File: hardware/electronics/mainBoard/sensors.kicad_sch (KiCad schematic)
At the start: 8 parts, among them J16 M8S-04PFFR-SF8001, J17 STEMMA-QT, J18 STEMMA-QT, J19 STEMMA-QT, J20 STEMMA-QT, J21 STEMMA-QT, U18 LPS28DFW

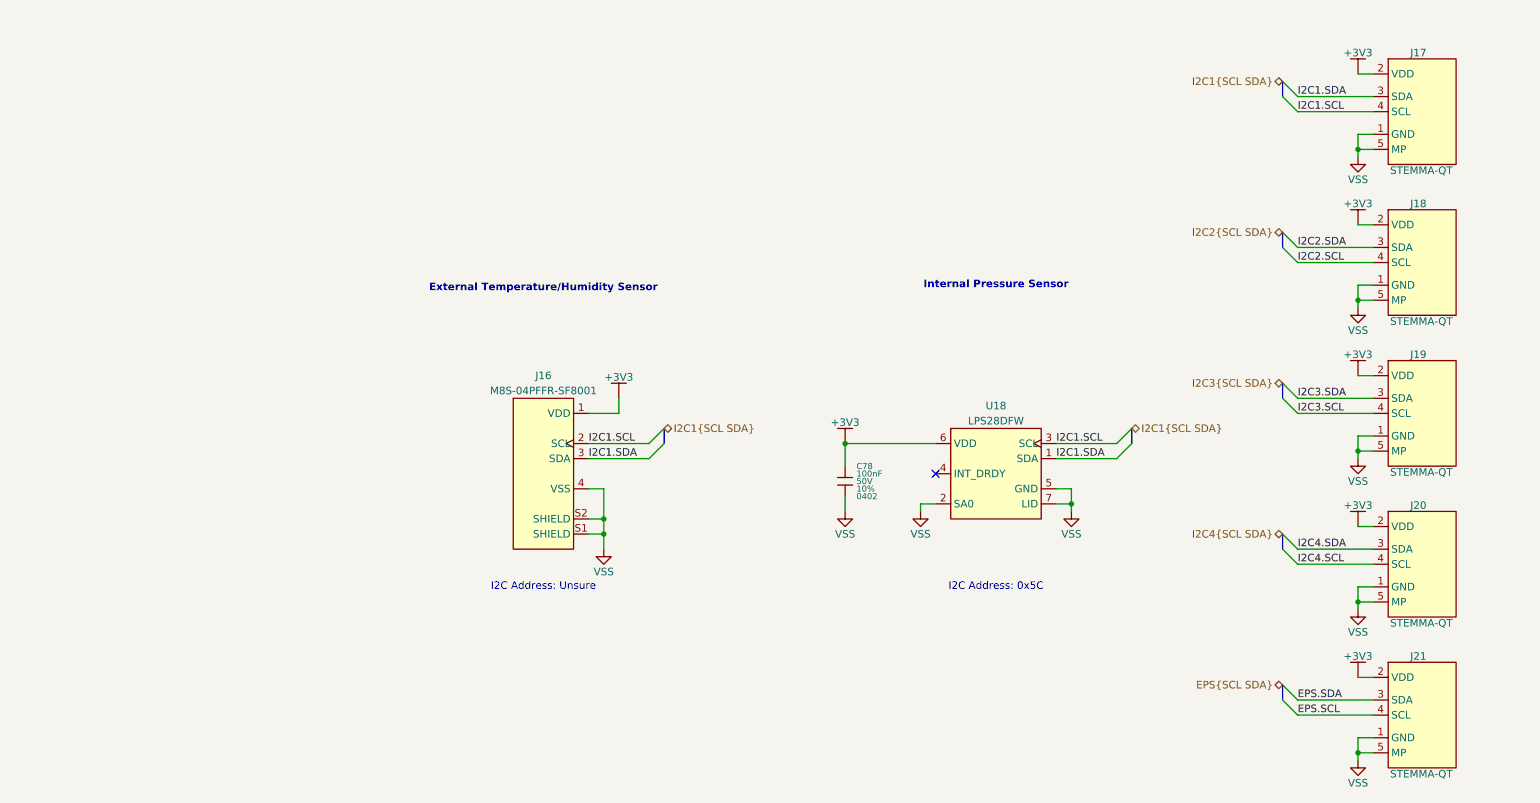
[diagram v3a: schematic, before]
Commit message: updated symbol refs
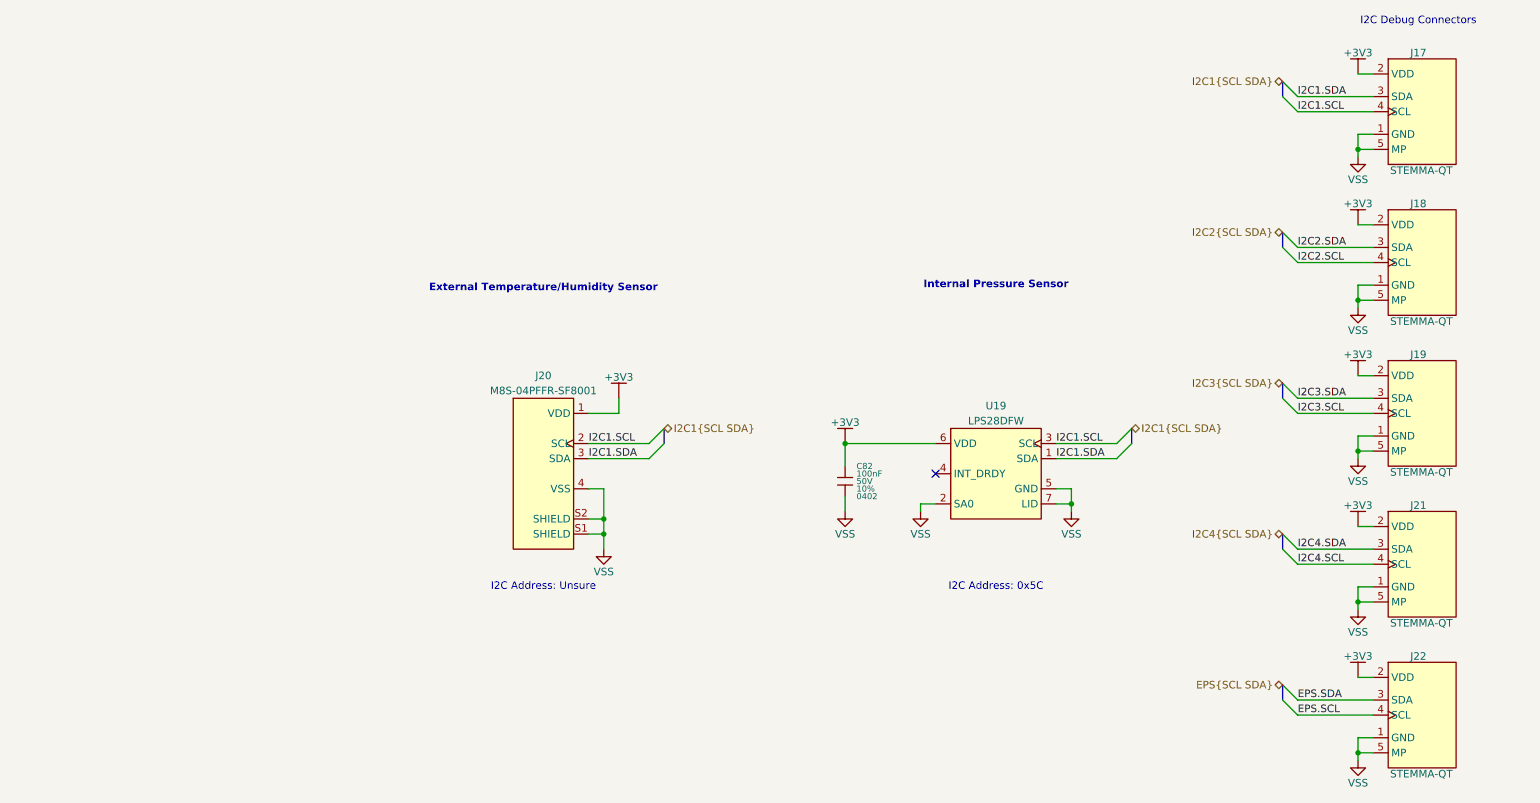
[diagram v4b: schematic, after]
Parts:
- renumbered C78 to C82, J16 to J20, J20 to J21, J21 to J22, U18 to U19
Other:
- note added: "I2C Debug Connectors"
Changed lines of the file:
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@@
+		)
+	)
+	(text "I2C Debug Connectors"
+		(exclude_from_sim no)
+		(at 248.92 31.75 0)
+		(effects
+			(font
+				(size 1.27 1.27)
+			)
 		)
 	)
@@
 		(dnp no)
 		(fields_autoplaced yes)
-		(property "Reference" "#PWR0187"
+		(property "Reference" "#PWR0186"
 			(at 238.76 54.61 0)
 			(effects
@@
 			(project "mainBoard"
 				(path "/be16e32f-2ccf-4272-9ec7-94d5fe7a55e0/4fa91b0b-0224-4171-b5d2-5ca4be681229"
-					(reference "#PWR0187")
+					(reference "#PWR0186")
 					(unit 1)
 				)
@@
 	)
 	(symbol
-		(lib_name "STEMMA-QT_1")
 		(lib_id "lib_sch:STEMMA-QT_1")
 		(at 246.38 148.59 0)
@@
 		(dnp no)
 		(fields_autoplaced yes)
-		(property "Reference" "J21"
+		(property "Reference" "J22"
 			(at 248.92 138.684 0)
 			(do_not_autoplace yes)
@@
 			(project "mainBoard"
 				(path "/be16e32f-2ccf-4272-9ec7-94d5fe7a55e0/4fa91b0b-0224-4171-b5d2-5ca4be681229"
-					(reference "J21")
+					(reference "J22")
 					(unit 1)
 				)
@@
 		(dnp no)
 		(fields_autoplaced yes)
-		(property "Reference" "#PWR0180"
+		(property "Reference" "#PWR0197"
 			(at 111.76 120.65 0)
 			(effects
@@
 			(project "mainBoard"
 				(path "/be16e32f-2ccf-4272-9ec7-94d5fe7a55e0/4fa91b0b-0224-4171-b5d2-5ca4be681229"
-					(reference "#PWR0180")
+					(reference "#PWR0197")
 					(unit 1)
 				)
@@
 	)
 	(symbol
-		(lib_name "STEMMA-QT_1")
 		(lib_id "lib_sch:STEMMA-QT_1")
 		(at 246.38 72.39 0)
@@
 	)
 	(symbol
-		(lib_name "STEMMA-QT_1")
 		(lib_id "lib_sch:STEMMA-QT_1")
 		(at 246.38 46.99 0)
@@
 	)
 	(symbol
-		(lib_name "STEMMA-QT_1")
 		(lib_id "lib_sch:STEMMA-QT_1")
 		(at 246.38 97.79 0)
@@
 		(dnp no)
 		(fields_autoplaced yes)
-		(property "Reference" "#PWR0193"
+		(property "Reference" "#PWR0198"
 			(at 238.76 130.81 0)
 			(effects
@@
 			(project "mainBoard"
 				(path "/be16e32f-2ccf-4272-9ec7-94d5fe7a55e0/4fa91b0b-0224-4171-b5d2-5ca4be681229"
-					(reference "#PWR0193")
+					(reference "#PWR0198")
 					(unit 1)
 				)
@@
 		(dnp no)
 		(fields_autoplaced yes)
-		(property "Reference" "#PWR0190"
+		(property "Reference" "#PWR0189"
 			(at 238.76 91.44 0)
 			(effects
@@
 			(project "mainBoard"
 				(path "/be16e32f-2ccf-4272-9ec7-94d5fe7a55e0/4fa91b0b-0224-4171-b5d2-5ca4be681229"
-					(reference "#PWR0190")
+					(reference "#PWR0189")
 					(unit 1)
 				)
@@
 		(dnp no)
 		(fields_autoplaced yes)
-		(property "Reference" "#PWR0195"
+		(property "Reference" "#PWR0200"
 			(at 238.76 156.21 0)
 			(effects
@@
 			(project "mainBoard"
 				(path "/be16e32f-2ccf-4272-9ec7-94d5fe7a55e0/4fa91b0b-0224-4171-b5d2-5ca4be681229"
-					(reference "#PWR0195")
+					(reference "#PWR0200")
 					(unit 1)
 				)
@@
 		(dnp no)
 		(fields_autoplaced yes)
-		(property "Reference" "#PWR0194"
+		(property "Reference" "#PWR0199"
 			(at 238.76 142.24 0)
 			(effects
@@
 			(project "mainBoard"
 				(path "/be16e32f-2ccf-4272-9ec7-94d5fe7a55e0/4fa91b0b-0224-4171-b5d2-5ca4be681229"
-					(reference "#PWR0194")
+					(reference "#PWR0199")
 					(unit 1)
 				)
@@
 		(dnp no)
 		(fields_autoplaced yes)
-		(property "Reference" "#PWR0189"
+		(property "Reference" "#PWR0188"
 			(at 238.76 80.01 0)
 			(effects
@@
 			(project "mainBoard"
 				(path "/be16e32f-2ccf-4272-9ec7-94d5fe7a55e0/4fa91b0b-0224-4171-b5d2-5ca4be681229"
-					(reference "#PWR0189")
+					(reference "#PWR0188")
 					(unit 1)
 				)
@@
 		(dnp no)
 		(fields_autoplaced yes)
-		(property "Reference" "#PWR0188"
+		(property "Reference" "#PWR0187"
 			(at 238.76 66.04 0)
 			(effects
@@
 			(project "mainBoard"
 				(path "/be16e32f-2ccf-4272-9ec7-94d5fe7a55e0/4fa91b0b-0224-4171-b5d2-5ca4be681229"
-					(reference "#PWR0188")
+					(reference "#PWR0187")
 					(unit 1)
 				)
@@
 		(dnp no)
 		(fields_autoplaced yes)
-		(property "Reference" "#PWR0183"
+		(property "Reference" "#PWR0193"
 			(at 152.4 114.3 0)
 			(effects
@@
 			(project "mainBoard"
 				(path "/be16e32f-2ccf-4272-9ec7-94d5fe7a55e0/4fa91b0b-0224-4171-b5d2-5ca4be681229"
-					(reference "#PWR0183")
+					(reference "#PWR0193")
 					(unit 1)
 				)
@@
 		(dnp no)
 		(fields_autoplaced yes)
-		(property "Reference" "C78"
+		(property "Reference" "C82"
 			(at 154.305 106.68 0)
 			(do_not_autoplace yes)
@@
 			(project "mainBoard"
 				(path "/be16e32f-2ccf-4272-9ec7-94d5fe7a55e0/4fa91b0b-0224-4171-b5d2-5ca4be681229"
-					(reference "C78")
+					(reference "C82")
 					(unit 1)
 				)
@@
 	)
 	(symbol
-		(lib_name "STEMMA-QT_1")
 		(lib_id "lib_sch:STEMMA-QT_1")
 		(at 246.38 123.19 0)
@@
 		(dnp no)
 		(fields_autoplaced yes)
-		(property "Reference" "J20"
+		(property "Reference" "J21"
 			(at 248.92 113.284 0)
 			(do_not_autoplace yes)
@@
 			(project "mainBoard"
 				(path "/be16e32f-2ccf-4272-9ec7-94d5fe7a55e0/4fa91b0b-0224-4171-b5d2-5ca4be681229"
-					(reference "J20")
+					(reference "J21")
 					(unit 1)
 				)
@@
 		(dnp no)
 		(fields_autoplaced yes)
-		(property "Reference" "#PWR0191"
+		(property "Reference" "#PWR0192"
 			(at 238.76 105.41 0)
 			(effects
@@
 			(project "mainBoard"
 				(path "/be16e32f-2ccf-4272-9ec7-94d5fe7a55e0/4fa91b0b-0224-4171-b5d2-5ca4be681229"
-					(reference "#PWR0191")
+					(reference "#PWR0192")
 					(unit 1)
 				)
@@
 		(dnp no)
 		(fields_autoplaced yes)
-		(property "Reference" "#PWR0181"
+		(property "Reference" "#PWR0190"
 			(at 114.3 95.25 0)
 			(effects
@@
 			(project "mainBoard"
 				(path "/be16e32f-2ccf-4272-9ec7-94d5fe7a55e0/4fa91b0b-0224-4171-b5d2-5ca4be681229"
-					(reference "#PWR0181")
+					(reference "#PWR0190")
 					(unit 1)
 				)
@@
 		(dnp no)
 		(fields_autoplaced yes)
-		(property "Reference" "J16"
+		(property "Reference" "J20"
 			(at 101.6 91.44 0)
 			(do_not_autoplace yes)
@@
 			(project "mainBoard"
 				(path "/be16e32f-2ccf-4272-9ec7-94d5fe7a55e0/4fa91b0b-0224-4171-b5d2-5ca4be681229"
-					(reference "J16")
+					(reference "J20")
 					(unit 1)
 				)
@@
 		(dnp no)
 		(fields_autoplaced yes)
-		(property "Reference" "#PWR0192"
+		(property "Reference" "#PWR0196"
 			(at 238.76 116.84 0)
 			(effects
@@
 			(project "mainBoard"
 				(path "/be16e32f-2ccf-4272-9ec7-94d5fe7a55e0/4fa91b0b-0224-4171-b5d2-5ca4be681229"
-					(reference "#PWR0192")
+					(reference "#PWR0196")
 					(unit 1)
 				)
@@
 		(dnp no)
 		(fields_autoplaced yes)
-		(property "Reference" "#PWR0185"
+		(property "Reference" "#PWR0195"
 			(at 190.5 114.3 0)
 			(effects
@@
 			(project "mainBoard"
 				(path "/be16e32f-2ccf-4272-9ec7-94d5fe7a55e0/4fa91b0b-0224-4171-b5d2-5ca4be681229"
-					(reference "#PWR0185")
+					(reference "#PWR0195")
 					(unit 1)
 				)
@@
 		(dnp no)
 		(fields_autoplaced yes)
-		(property "Reference" "U18"
+		(property "Reference" "U19"
 			(at 177.8 96.52 0)
 			(do_not_autoplace yes)
@@
 			(project "mainBoard"
 				(path "/be16e32f-2ccf-4272-9ec7-94d5fe7a55e0/4fa91b0b-0224-4171-b5d2-5ca4be681229"
-					(reference "U18")
+					(reference "U19")
 					(unit 1)
 				)
@@
 		(dnp no)
 		(fields_autoplaced yes)
-		(property "Reference" "#PWR0182"
+		(property "Reference" "#PWR0191"
 			(at 152.4 102.87 0)
 			(effects
@@
 			(project "mainBoard"
 				(path "/be16e32f-2ccf-4272-9ec7-94d5fe7a55e0/4fa91b0b-0224-4171-b5d2-5ca4be681229"
-					(reference "#PWR0182")
+					(reference "#PWR0191")
 					(unit 1)
 				)
@@
 		(dnp no)
 		(fields_autoplaced yes)
-		(property "Reference" "#PWR0184"
+		(property "Reference" "#PWR0194"
 			(at 165.1 114.3 0)
 			(effects
@@
 			(project "mainBoard"
 				(path "/be16e32f-2ccf-4272-9ec7-94d5fe7a55e0/4fa91b0b-0224-4171-b5d2-5ca4be681229"
-					(reference "#PWR0184")
+					(reference "#PWR0194")
 					(unit 1)
 				)
@@
 		(dnp no)
 		(fields_autoplaced yes)
-		(property "Reference" "#PWR0186"
+		(property "Reference" "#PWR0185"
 			(at 238.76 40.64 0)
 			(effects
@@
 			(project "mainBoard"
 				(path "/be16e32f-2ccf-4272-9ec7-94d5fe7a55e0/4fa91b0b-0224-4171-b5d2-5ca4be681229"
-					(reference "#PWR0186")
+					(reference "#PWR0185")
 					(unit 1)
 				)

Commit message: assigned FPs
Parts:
- J17, J18, J19, J21, J22: footprint (none) -> lib_connectors:JST_SH_BM04B-SRSS-TB
- J20: footprint (none) -> lib_connectors:M8S-04PFFR-SF8001
- U19: footprint (none) -> lib_ICs:CCLGA7_LPS28DFWTR
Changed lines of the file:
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@@
 			)
 		)
-		(property "Footprint" ""
+		(property "Footprint" "lib_connectors:JST_SH_BM04B-SRSS-TB"
 			(at 241.3 142.24 0)
 			(effects
@@
 			)
 		)
-		(property "Footprint" ""
+		(property "Footprint" "lib_connectors:JST_SH_BM04B-SRSS-TB"
 			(at 241.3 66.04 0)
 			(effects
@@
 			)
 		)
-		(property "Footprint" ""
+		(property "Footprint" "lib_connectors:JST_SH_BM04B-SRSS-TB"
 			(at 241.3 40.64 0)
 			(effects
@@
 			)
 		)
-		(property "Footprint" ""
+		(property "Footprint" "lib_connectors:JST_SH_BM04B-SRSS-TB"
 			(at 241.3 91.44 0)
 			(effects
@@
 			)
 		)
-		(property "Footprint" ""
+		(property "Footprint" "lib_connectors:JST_SH_BM04B-SRSS-TB"
 			(at 241.3 116.84 0)
 			(effects
@@
 			)
 		)
-		(property "Footprint" ""
+		(property "Footprint" "lib_connectors:M8S-04PFFR-SF8001"
 			(at 101.6 107.95 0)
 			(effects
@@
 			)
 		)
-		(property "Footprint" ""
+		(property "Footprint" "lib_ICs:CCLGA7_LPS28DFWTR"
 			(at 177.8 107.95 0)
 			(effects

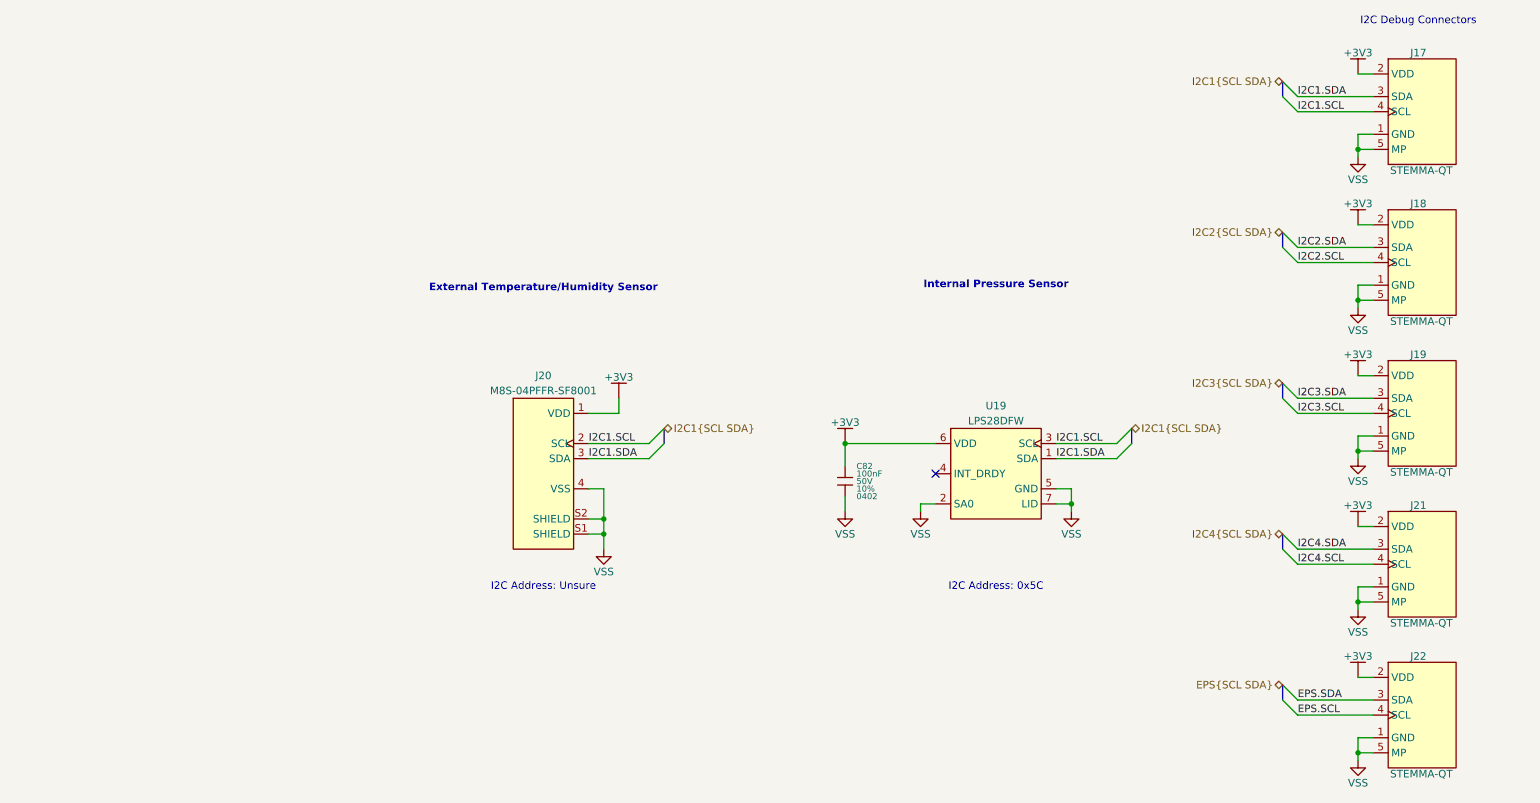
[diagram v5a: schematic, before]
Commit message: assigned footprints
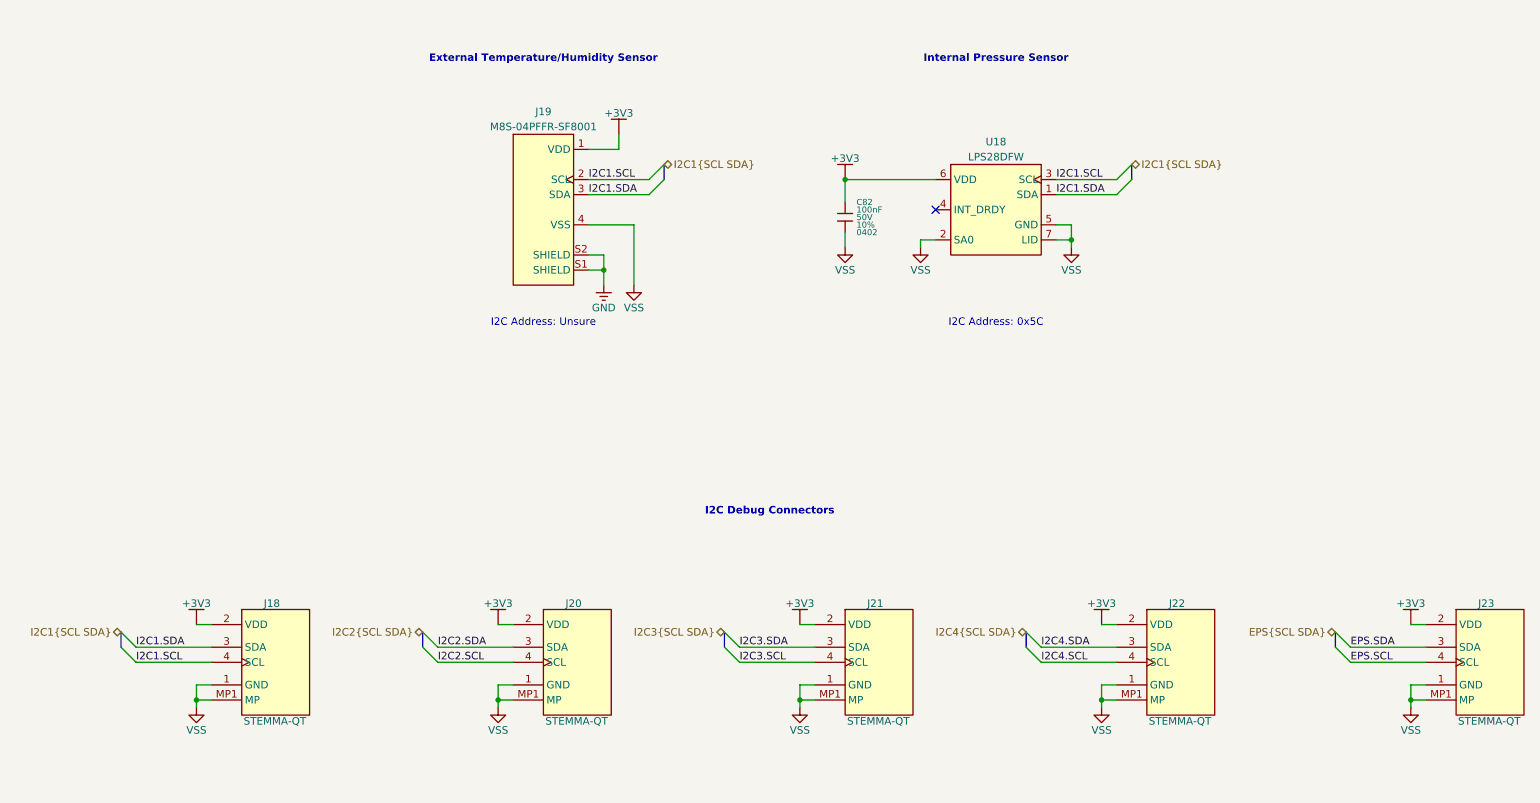
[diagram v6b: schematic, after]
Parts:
- removed J17, J18, J19, J21, J22: STEMMA-QT, lib_connectors:JST_SH_BM04B-SRSS-TB, symbol lib_sch:STEMMA-QT_1
- added J18, J20, J21, J22, J23: STEMMA-QT, lib_connectors:JST_SH_BM04B-SRSS-TB, symbol lib_sch:STEMMA-QT
- C82: footprint (none) -> lib_passives:GCM0402
- renumbered J20 to J19, U19 to U18
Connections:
- net +3V3: now also J18.2 (VDD), J20.2 (VDD), J21.2 (VDD), J22.2 (VDD), J23.2 (VDD)
- net EPS.SCL: now also J23.4 (SCL)
- net EPS.SDA: now also J23.3 (SDA)
- net I2C1.SCL: now also J18.4 (SCL)
- net I2C1.SDA: now also J18.3 (SDA)
- net I2C2.SCL: now also J20.4 (SCL)
- net I2C2.SDA: now also J20.3 (SDA)
- net I2C3.SCL: now also J21.4 (SCL)
- net I2C3.SDA: now also J21.3 (SDA)
- net I2C4.SCL: now also J22.4 (SCL)
- net I2C4.SDA: now also J22.3 (SDA)
- net VSS: now also J18.1 (GND), J18.MP1 (MP), J18.MP2 (MP), J20.1 (GND), J20.MP1 (MP), J20.MP2 (MP), J21.1 (GND), J21.MP1 (MP), J21.MP2 (MP), J22.1 (GND), J22.MP1 (MP), J22.MP2 (MP), J23.1 (GND), J23.MP1 (MP), J23.MP2 (MP); no longer J19.S1 (SHIELD), J19.S2 (SHIELD)
- new net GND: J19.S1 (SHIELD), J19.S2 (SHIELD)
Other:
- moved on the sheet: C82, J19, U18
